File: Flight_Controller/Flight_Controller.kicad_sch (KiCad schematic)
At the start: 0 parts

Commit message: Set footprints
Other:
- added sheet MCU/Connectors (MCU.kicad_sch)
- added sheet Peripherals/Power (Peripherals.kicad_sch)

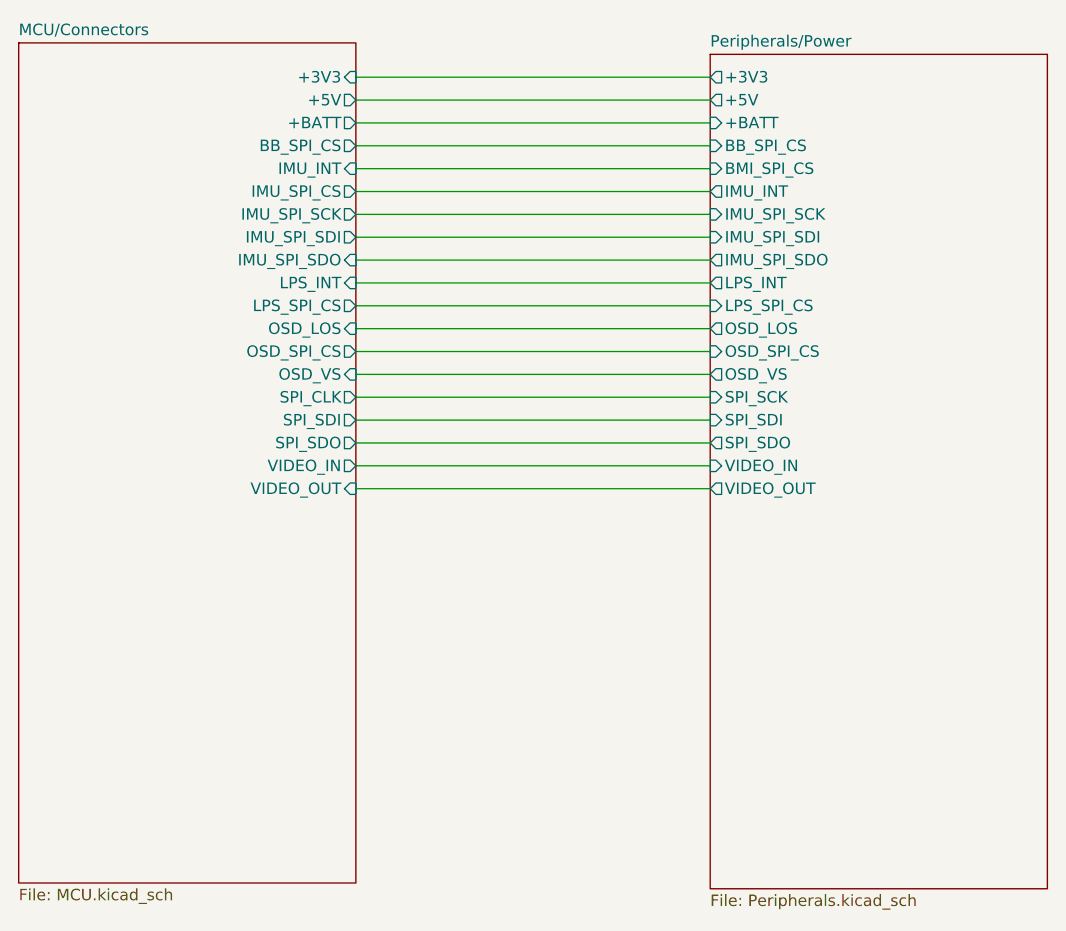
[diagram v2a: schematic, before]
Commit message: Made schem look nicer
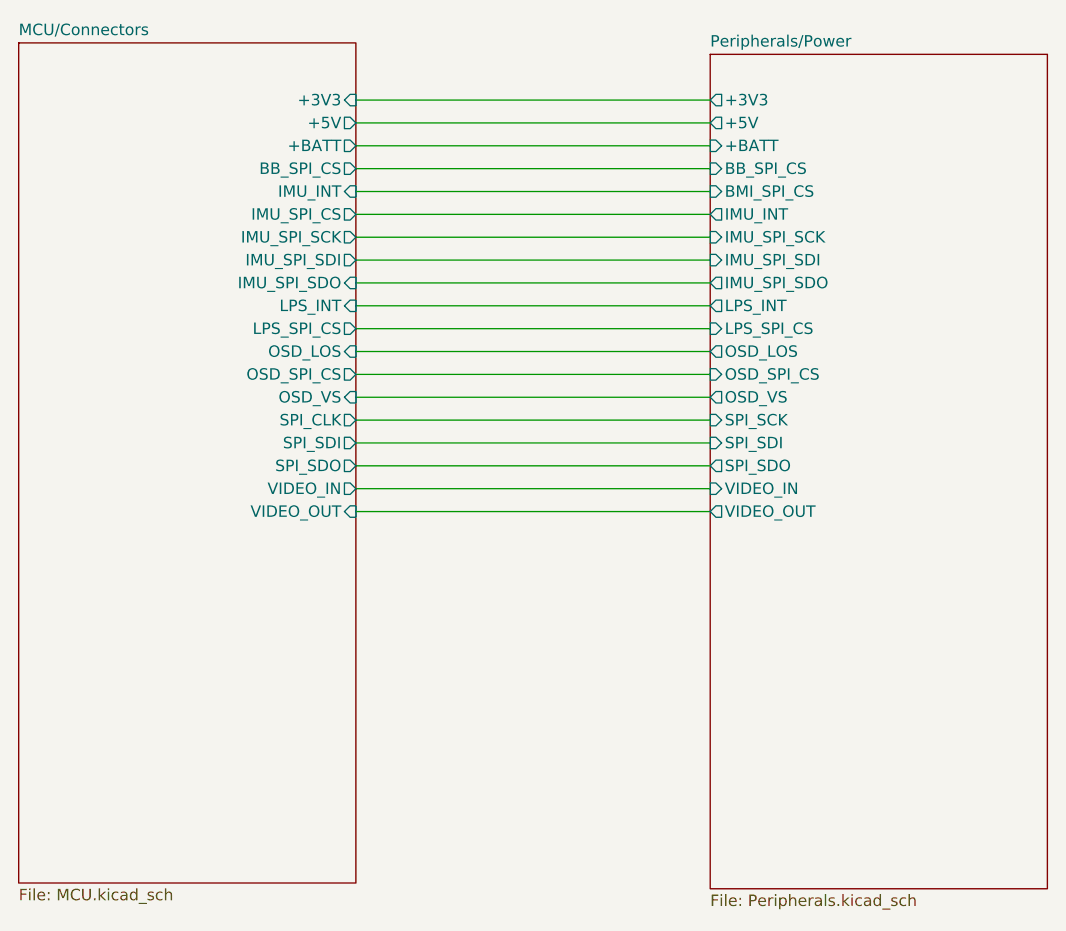
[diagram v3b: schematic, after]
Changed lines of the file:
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@@
 	(wire
 		(pts
-			(xy 54.61 113.03) (xy 93.98 113.03)
+			(xy 54.61 115.57) (xy 93.98 115.57)
 		)
 		(stroke
@@
 	(wire
 		(pts
-			(xy 54.61 118.11) (xy 93.98 118.11)
+			(xy 54.61 120.65) (xy 93.98 120.65)
 		)
 		(stroke
@@
 	(wire
 		(pts
-			(xy 54.61 148.59) (xy 93.98 148.59)
+			(xy 54.61 151.13) (xy 93.98 151.13)
 		)
 		(stroke
@@
 	(wire
 		(pts
-			(xy 54.61 143.51) (xy 93.98 143.51)
+			(xy 54.61 146.05) (xy 93.98 146.05)
 		)
 		(stroke
@@
 	(wire
 		(pts
-			(xy 54.61 128.27) (xy 93.98 128.27)
+			(xy 54.61 130.81) (xy 93.98 130.81)
 		)
 		(stroke
@@
 	(wire
 		(pts
-			(xy 54.61 135.89) (xy 93.98 135.89)
+			(xy 54.61 138.43) (xy 93.98 138.43)
 		)
 		(stroke
@@
 	(wire
 		(pts
-			(xy 54.61 146.05) (xy 93.98 146.05)
+			(xy 54.61 148.59) (xy 93.98 148.59)
 		)
 		(stroke
@@
 	(wire
 		(pts
-			(xy 54.61 102.87) (xy 93.98 102.87)
+			(xy 54.61 105.41) (xy 93.98 105.41)
 		)
 		(stroke
@@
 	(wire
 		(pts
-			(xy 54.61 123.19) (xy 93.98 123.19)
+			(xy 54.61 125.73) (xy 93.98 125.73)
 		)
 		(stroke
@@
 	(wire
 		(pts
-			(xy 54.61 140.97) (xy 93.98 140.97)
+			(xy 54.61 143.51) (xy 93.98 143.51)
 		)
 		(stroke
@@
 	(wire
 		(pts
-			(xy 54.61 125.73) (xy 93.98 125.73)
+			(xy 54.61 128.27) (xy 93.98 128.27)
 		)
 		(stroke
@@
 	(wire
 		(pts
-			(xy 54.61 130.81) (xy 93.98 130.81)
+			(xy 54.61 133.35) (xy 93.98 133.35)
 		)
 		(stroke
@@
 	(wire
 		(pts
-			(xy 54.61 115.57) (xy 93.98 115.57)
+			(xy 54.61 118.11) (xy 93.98 118.11)
 		)
 		(stroke
@@
 	(wire
 		(pts
-			(xy 54.61 138.43) (xy 93.98 138.43)
+			(xy 54.61 140.97) (xy 93.98 140.97)
 		)
 		(stroke
@@
 	(wire
 		(pts
-			(xy 54.61 105.41) (xy 93.98 105.41)
+			(xy 54.61 107.95) (xy 93.98 107.95)
 		)
 		(stroke
@@
 	(wire
 		(pts
-			(xy 54.61 110.49) (xy 93.98 110.49)
+			(xy 54.61 113.03) (xy 93.98 113.03)
 		)
 		(stroke
@@
 	(wire
 		(pts
-			(xy 54.61 120.65) (xy 93.98 120.65)
+			(xy 54.61 123.19) (xy 93.98 123.19)
 		)
 		(stroke
@@
 	(wire
 		(pts
-			(xy 54.61 133.35) (xy 93.98 133.35)
+			(xy 54.61 135.89) (xy 93.98 135.89)
 		)
 		(stroke
@@
 	(wire
 		(pts
-			(xy 54.61 107.95) (xy 93.98 107.95)
+			(xy 54.61 110.49) (xy 93.98 110.49)
 		)
 		(stroke
@@
 		)
 		(pin "+3V3" input
-			(at 54.61 102.87 0)
+			(at 54.61 105.41 0)
 			(effects
 				(font
@@
 		)
 		(pin "+5V" output
-			(at 54.61 105.41 0)
+			(at 54.61 107.95 0)
 			(effects
 				(font
@@
 		)
 		(pin "+BATT" output
-			(at 54.61 107.95 0)
+			(at 54.61 110.49 0)
 			(effects
 				(font
@@
 		)
 		(pin "BB_SPI_CS" output
-			(at 54.61 110.49 0)
+			(at 54.61 113.03 0)
 			(effects
 				(font
@@
 		)
 		(pin "IMU_INT" input
-			(at 54.61 113.03 0)
+			(at 54.61 115.57 0)
 			(effects
 				(font
@@
 		)
 		(pin "IMU_SPI_CS" output
-			(at 54.61 115.57 0)
+			(at 54.61 118.11 0)
 			(effects
 				(font
@@
 		)
 		(pin "IMU_SPI_SCK" output
-			(at 54.61 118.11 0)
+			(at 54.61 120.65 0)
 			(effects
 				(font
@@
 		)
 		(pin "IMU_SPI_SDI" output
-			(at 54.61 120.65 0)
+			(at 54.61 123.19 0)
 			(effects
 				(font
@@
 		)
 		(pin "IMU_SPI_SDO" input
-			(at 54.61 123.19 0)
+			(at 54.61 125.73 0)
 			(effects
 				(font
@@
 		)
 		(pin "LPS_INT" input
-			(at 54.61 125.73 0)
+			(at 54.61 128.27 0)
 			(effects
 				(font
@@
 		)
 		(pin "LPS_SPI_CS" output
-			(at 54.61 128.27 0)
+			(at 54.61 130.81 0)
 			(effects
 				(font
@@
 		)
 		(pin "OSD_LOS" input
-			(at 54.61 130.81 0)
+			(at 54.61 133.35 0)
 			(effects
 				(font
@@
 		)
 		(pin "OSD_SPI_CS" output
-			(at 54.61 133.35 0)
+			(at 54.61 135.89 0)
 			(effects
 				(font
@@
 		)
 		(pin "OSD_VS" input
-			(at 54.61 135.89 0)
+			(at 54.61 138.43 0)
 			(effects
 				(font
@@
 		)
 		(pin "SPI_CLK" output
-			(at 54.61 138.43 0)
+			(at 54.61 140.97 0)
 			(effects
 				(font
@@
 		)
 		(pin "SPI_SDI" output
-			(at 54.61 140.97 0)
+			(at 54.61 143.51 0)
 			(effects
 				(font
@@
 		)
 		(pin "SPI_SDO" output
-			(at 54.61 143.51 0)
+			(at 54.61 146.05 0)
 			(effects
 				(font
@@
 		)
 		(pin "VIDEO_IN" output
-			(at 54.61 146.05 0)
+			(at 54.61 148.59 0)
 			(effects
 				(font
@@
 		)
 		(pin "VIDEO_OUT" input
-			(at 54.61 148.59 0)
+			(at 54.61 151.13 0)
 			(effects
 				(font
@@
 		)
 		(pin "+3V3" output
-			(at 93.98 102.87 180)
+			(at 93.98 105.41 180)
 			(effects
 				(font
@@
 		)
 		(pin "+5V" output
-			(at 93.98 105.41 180)
+			(at 93.98 107.95 180)
 			(effects
 				(font
@@
 		)
 		(pin "+BATT" input
-			(at 93.98 107.95 180)
+			(at 93.98 110.49 180)
 			(effects
 				(font
@@
 		)
 		(pin "BB_SPI_CS" input
-			(at 93.98 110.49 180)
+			(at 93.98 113.03 180)
 			(effects
 				(font
@@
 		)
 		(pin "BMI_SPI_CS" input
-			(at 93.98 113.03 180)
+			(at 93.98 115.57 180)
 			(effects
 				(font
@@
 		)
 		(pin "IMU_INT" output
-			(at 93.98 115.57 180)
+			(at 93.98 118.11 180)
 			(effects
 				(font
@@
 		)
 		(pin "IMU_SPI_SCK" input
-			(at 93.98 118.11 180)
+			(at 93.98 120.65 180)
 			(effects
 				(font
@@
 		)
 		(pin "IMU_SPI_SDI" input
-			(at 93.98 120.65 180)
+			(at 93.98 123.19 180)
 			(effects
 				(font
@@
 		)
 		(pin "IMU_SPI_SDO" output
-			(at 93.98 123.19 180)
+			(at 93.98 125.73 180)
 			(effects
 				(font
@@
 		)
 		(pin "LPS_INT" output
-			(at 93.98 125.73 180)
+			(at 93.98 128.27 180)
 			(effects
 				(font
@@
 		)
 		(pin "LPS_SPI_CS" input
-			(at 93.98 128.27 180)
+			(at 93.98 130.81 180)
 			(effects
 				(font
@@
 		)
 		(pin "OSD_LOS" output
-			(at 93.98 130.81 180)
+			(at 93.98 133.35 180)
 			(effects
 				(font
@@
 		)
 		(pin "OSD_SPI_CS" input
-			(at 93.98 133.35 180)
+			(at 93.98 135.89 180)
 			(effects
 				(font
@@
 		)
 		(pin "OSD_VS" output
-			(at 93.98 135.89 180)
+			(at 93.98 138.43 180)
 			(effects
 				(font
@@
 		)
 		(pin "SPI_SCK" input
-			(at 93.98 138.43 180)
+			(at 93.98 140.97 180)
 			(effects
 				(font
@@
 		)
 		(pin "SPI_SDI" input
-			(at 93.98 140.97 180)
+			(at 93.98 143.51 180)
 			(effects
 				(font
@@
 		)
 		(pin "SPI_SDO" output
-			(at 93.98 143.51 180)
+			(at 93.98 146.05 180)
 			(effects
 				(font
@@
 		)
 		(pin "VIDEO_IN" input
-			(at 93.98 146.05 180)
+			(at 93.98 148.59 180)
 			(effects
 				(font
@@
 		)
 		(pin "VIDEO_OUT" output
-			(at 93.98 148.59 180)
+			(at 93.98 151.13 180)
 			(effects
 				(font
